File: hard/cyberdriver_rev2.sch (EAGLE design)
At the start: 28 parts, among them IC1 OPAMP-DUALU, Q1 MOSFET-NCHANNELBSS123LT1G, U1 ATTINY2313A

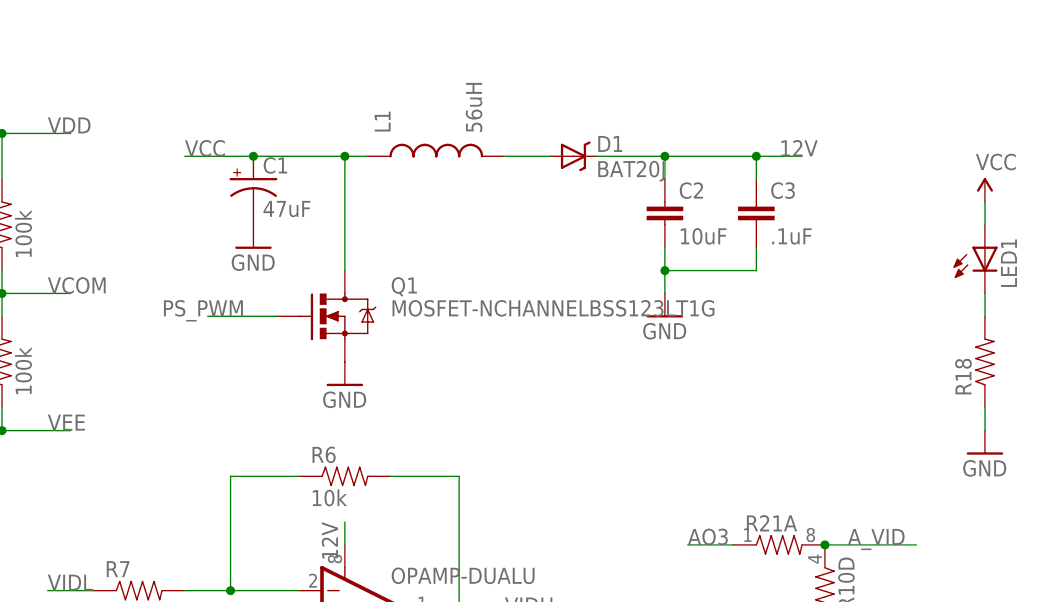
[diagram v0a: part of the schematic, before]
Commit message: Firmware started (ps working, adc sort of) hardware rev2 started
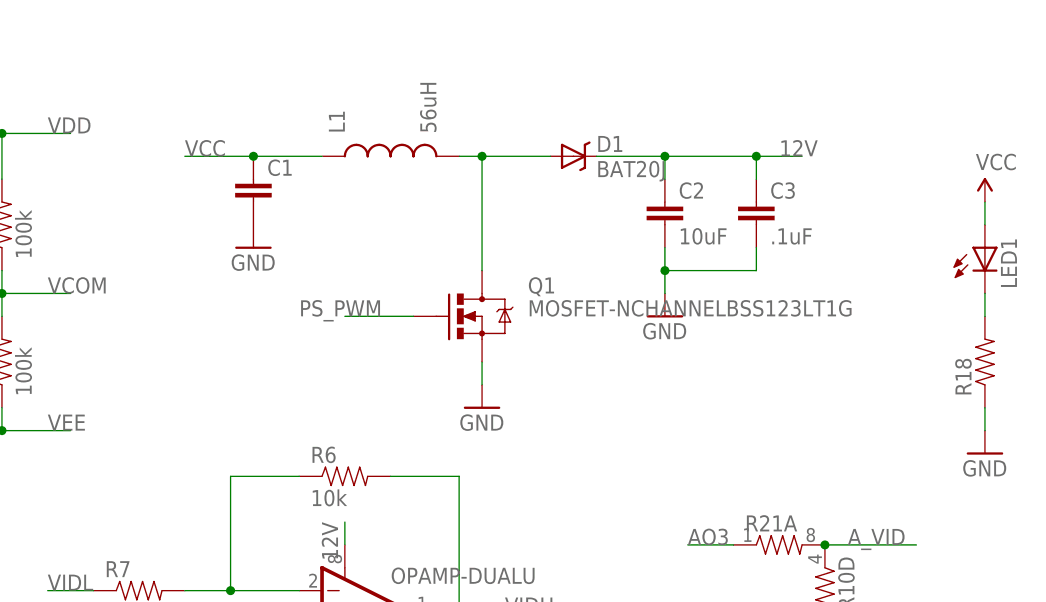
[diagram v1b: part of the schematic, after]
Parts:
- C1: value 47uF -> (none); device cyberdriver:CAP_POLC -> SparkFun-Capacitors:CAP1206
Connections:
- net GND: now also C1.2; no longer C1.-
- net N$4: now also Q1.D
- net VCC: now also C1.1; no longer C1.+, Q1.D
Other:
- moved on the sheet: L1, Q1
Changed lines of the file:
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@@
 <part name="R9" library="cyberdriver" deviceset="RESISTOR" device="0603-RES" value="10k"/>
 <part name="L1" library="cyberdriver" deviceset="INDUCTOR" device="SDR0403-560KL" value="56uH"/>
-<part name="C1" library="cyberdriver" deviceset="CAP_POL" device="C" value="47uF"/>
 <part name="GND6" library="cyberdriver" deviceset="GND" device=""/>
 <part name="GND7" library="cyberdriver" deviceset="GND" device=""/>
@@
 <part name="R10" library="SparkFun-Passives" deviceset="RESISTOR-ARRAY" device="0603-ARV"/>
 <part name="JP2" library="SparkFun-Passives" deviceset="JUMPER-3" device="SMD"/>
+<part name="C1" library="SparkFun-Capacitors" deviceset="CAP" device="1206"/>
 </parts>
 <sheets>
@@
 <instance part="R8" gate="G$1" x="147.32" y="2.54" rot="R90"/>
 <instance part="R9" gate="G$1" x="160.02" y="7.62" rot="R180"/>
-<instance part="L1" gate="G$1" x="167.64" y="99.06" rot="R90"/>
-<instance part="C1" gate="G$1" x="147.32" y="96.52"/>
+<instance part="L1" gate="G$1" x="162.56" y="99.06" rot="R90"/>
 <instance part="GND6" gate="1" x="147.32" y="88.9"/>
-<instance part="GND7" gate="1" x="157.48" y="73.66"/>
+<instance part="GND7" gate="1" x="172.72" y="71.12"/>
 <instance part="GND8" gate="1" x="193.04" y="81.28"/>
-<instance part="Q1" gate="G$1" x="157.48" y="81.28"/>
+<instance part="Q1" gate="G$1" x="172.72" y="81.28"/>
 <instance part="GND9" gate="1" x="210.82" y="12.7"/>
 <instance part="JP1" gate="G$1" x="-35.56" y="-2.54"/>
@@
 <instance part="R10" gate="A" x="210.82" y="20.32" rot="R270"/>
 <instance part="JP2" gate="G$1" x="68.58" y="83.82" rot="R90"/>
+<instance part="C1" gate="G$1" x="147.32" y="93.98"/>
 </instances>
 <busses>
@@
 <pinref part="GND7" gate="1" pin="GND"/>
 <pinref part="Q1" gate="G$1" pin="S"/>
-</segment>
-<segment>
-<pinref part="C1" gate="G$1" pin="-"/>
-<pinref part="GND6" gate="1" pin="GND"/>
+<wire x1="172.72" y1="76.2" x2="172.72" y2="73.66" width="0.1524" layer="91"/>
 </segment>
 <segment>
@@
 <pinref part="R10" gate="A" pin="2"/>
 </segment>
+<segment>
+<pinref part="GND6" gate="1" pin="GND"/>
+<pinref part="C1" gate="G$1" pin="2"/>
+</segment>
 </net>
 <net name="VCC" class="0">
@@
 </segment>
 <segment>
-<pinref part="Q1" gate="G$1" pin="D"/>
-<wire x1="157.48" y1="86.36" x2="157.48" y2="99.06" width="0.1524" layer="91"/>
 <pinref part="L1" gate="G$1" pin="1"/>
-<wire x1="157.48" y1="99.06" x2="160.02" y2="99.06" width="0.1524" layer="91"/>
-<wire x1="157.48" y1="99.06" x2="147.32" y2="99.06" width="0.1524" layer="91"/>
-<pinref part="C1" gate="G$1" pin="+"/>
+<wire x1="154.94" y1="99.06" x2="147.32" y2="99.06" width="0.1524" layer="91"/>
+<label x="139.7" y="99.06" size="1.778" layer="95"/>
+<pinref part="C1" gate="G$1" pin="1"/>
+<wire x1="147.32" y1="99.06" x2="139.7" y2="99.06" width="0.1524" layer="91"/>
 <junction x="147.32" y="99.06"/>
-<wire x1="147.32" y1="99.06" x2="139.7" y2="99.06" width="0.1524" layer="91"/>
-<junction x="157.48" y="99.06"/>
-<label x="139.7" y="99.06" size="1.778" layer="95"/>
 </segment>
 <segment>
@@
 <segment>
 <pinref part="Q1" gate="G$1" pin="G"/>
-<wire x1="149.86" y1="81.28" x2="142.24" y2="81.28" width="0.1524" layer="91"/>
-<label x="137.16" y="81.28" size="1.778" layer="95"/>
+<wire x1="165.1" y1="81.28" x2="157.48" y2="81.28" width="0.1524" layer="91"/>
+<label x="152.4" y="81.28" size="1.778" layer="95"/>
 </segment>
 </net>
@@
 <pinref part="L1" gate="G$1" pin="2"/>
 <pinref part="D1" gate="G$1" pin="A"/>
-<wire x1="175.26" y1="99.06" x2="180.34" y2="99.06" width="0.1524" layer="91"/>
-</segment>
-</net>
+<wire x1="170.18" y1="99.06" x2="172.72" y2="99.06" width="0.1524" layer="91"/>
+<pinref part="Q1" gate="G$1" pin="D"/>
+<wire x1="172.72" y1="99.06" x2="180.34" y2="99.06" width="0.1524" layer="91"/>
+<wire x1="172.72" y1="86.36" x2="172.72" y2="99.06" width="0.1524" layer="91"/>
+<junction x="172.72" y="99.06"/>
+</segment>
+</net>
